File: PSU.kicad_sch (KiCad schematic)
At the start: 10 parts, among them J1 Mini USB Female, J4 Battery Connector, SW1 Screw Switch, U2 AMS1117-3.3

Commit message: Experimented with git
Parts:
- R8: value 470 -> 100
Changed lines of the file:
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@@
       (effects (font (size 1.27 1.27)) (justify left))
     )
-    (property "Value" "470" (id 1) (at 177.8 82.5499 0)
+    (property "Value" "100" (id 1) (at 177.8 82.5499 0)
       (effects (font (size 1.27 1.27)) (justify left))
     )

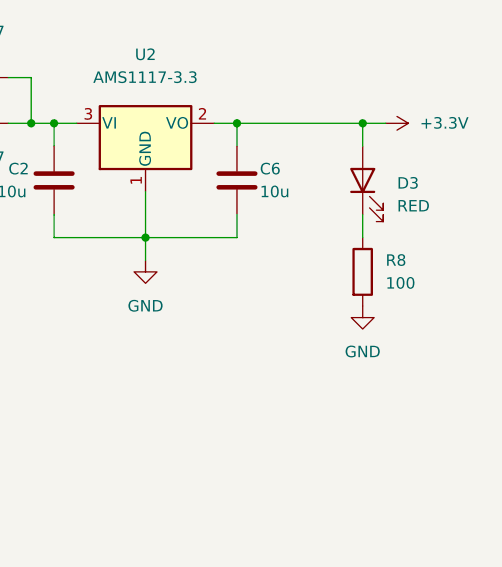
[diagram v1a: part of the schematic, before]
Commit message: Changed pullup resistor on power LED
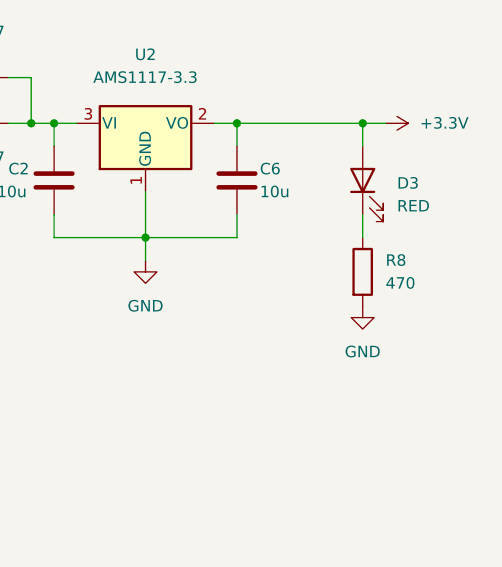
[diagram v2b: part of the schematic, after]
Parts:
- R8: value 100 -> 470
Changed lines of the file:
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@@
       (effects (font (size 1.27 1.27)) (justify left))
     )
-    (property "Value" "100" (id 1) (at 177.8 82.5499 0)
+    (property "Value" "470" (id 1) (at 177.8 82.5499 0)
       (effects (font (size 1.27 1.27)) (justify left))
     )
